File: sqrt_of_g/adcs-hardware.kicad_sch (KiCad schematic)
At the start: 29 parts, among them J10 35362-0650, J11 Conn_01x10, J12 353620850, J13 35362-0650, J14 353621050, J15 Conn_01x10, J16 35362-0650, J17 Conn_01x10, J18 35362-0650, J19 353621050, J20 353621050, J21 Conn_01x06, J22 Conn_01x06, J23 Conn_01x06, J24 Conn_01x06, J25 Conn_01x06, J26 Conn_01x06, J27 Conn_01x10, J28 35362-0650, J6 Conn_01x06, J7 Conn_01x08, J8 Conn_01x10, J9 35362-0650

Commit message: update board
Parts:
- J11, J15, J17, J27, J8: footprint (none) -> Connector_PinHeader_1.27mm:PinHeader_1x10_P1.27mm_Vertical
- J14: value 353621050 -> Thruster
- J21, J22, J23, J24, J25, J26: footprint (none) -> mainboard:MOLEX_35362-0650
- J7: footprint (none) -> Connector_PinHeader_2.54mm:PinHeader_1x08_P2.54mm_Vertical
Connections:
- net RX_ADCS renamed RX_FROM_PYCUBED
- net TX_ADCS renamed TX_TO_PYCUBED
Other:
- sheet GPS ports: added RX_FROM_MICRO, TX_TO_MICRO; removed RX_GPS, TX_GPS
- note added: "2-3. Add jumpers to allow USB battery power to Teensy (for programming). DO NOT USE TO POWER THRUSTER, COILS, or WHEELS."
- note added: "@GRANT this uses a sheet field to pass in 100k for the source resistor"
- note added: "Connector allows the RBFs placement on a side panel"
- note added: "LDO for analog 3V3 supply? add inductor, caps to filter things out? Should I make an analog GND plane? I feel like I am fine."
- note added: "LPUART4"
- note added: "Power Harness and Power Enable"
- note added: "RBF Jumpers / Harness"
- note added: "This power enable can hard reset the whole board."
- note removed: "2-3. Add jumper to allow USB battery power to wheels, coils. DO NOT USE TO POWER THRUSTER"
- note removed: "@GRANT this uses a sheet field to pass in 100k for the source resistor Somewhat related: should we power this from VBATT_IN (to avoid having two enables in series )? This is already after the foot switches"
- note removed: "ADCS Enable"
- note removed: "Connector allows the RBFs to be placed on a side panel"
- note removed: "From the board's POV, this is where it recieves and transmits. These must be flipped on the PyCubed side"
- note removed: "LDO for analog 3V3 supply? add inductor, caps to filter things out? Should I make an analog GND? I feel like I am fine."
- note removed: "RBF Jumpers"

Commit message: update main board
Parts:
- removed J10, J13, J16, J18: 35362-0650, mainboard:MOLEX_35362-0650, symbol mainboard:35362-0650
- removed J15, J17, J8: Conn_01x10, Connector_PinHeader_1.27mm:PinHeader_1x10_P1.27mm_Vertical, symbol Connector_Generic:Conn_01x10
- removed J19, J20: 353621050, CON_353621050, symbol adcs:353621050
- added H1, H2, H3, H4: MountingHole_Pad, MountingHole:MountingHole_3.2mm_M3_DIN965_Pad, symbol Mechanical:MountingHole_Pad
- added J1, J2: 353620650, mainboard:MOLEX_35362-0650, symbol mainboard:35362-0650
- added J12, J13, J14: Conn_01x10, Connector_PinHeader_2.54mm:PinHeader_1x10_P2.54mm_Vertical, symbol Connector_Generic:Conn_01x10
- added J3, J4: 353620850, adcs:SHDR8W50P0X200_1X8_1830X550X850P, symbol Connector_Generic:Conn_01x08
- added L1: 330uH, adcs:IND_SRN6045TA-331K, symbol Device:L
- J10: renamed from J14; value Thruster -> Thruster Connector; Flight (none) -> 353621050; Manufacturer_Name (none) -> Molex
- J11: footprint Connector_PinHeader_1.27mm:PinHeader_1x10_P1.27mm_Vertical -> Connector_PinHeader_2.54mm:PinHeader_1x10_P2.54mm_Vertical
- J15: renamed from J23; value Conn_01x06 -> 353620650; Flight (none) -> 353620650; Manufacturer_Name (none) -> Molex
- J16: renamed from J24; value Conn_01x06 -> 353620650; Flight (none) -> 353620650; Manufacturer_Name (none) -> Molex
- J17: renamed from J21; value Conn_01x06 -> 353620650; Flight (none) -> 353620650; Manufacturer_Name (none) -> Molex
- J18: renamed from J22; value Conn_01x06 -> 353620650; Flight (none) -> 353620650; Manufacturer_Name (none) -> Molex
- J19: renamed from J25; value Conn_01x06 -> 353620650; Flight (none) -> 353620650; Manufacturer_Name (none) -> Molex
- J20: renamed from J26; value Conn_01x06 -> 353620650; Flight (none) -> 353620650; Manufacturer_Name (none) -> Molex
- J21: renamed from J27; footprint Connector_PinHeader_1.27mm:PinHeader_1x10_P1.27mm_Vertical -> Connector_PinHeader_2.54mm:PinHeader_1x10_P2.54mm_Vertical
- J5: renamed from J28; value 35362-0650 -> 353620650; Flight (none) -> 353620650; Manufacturer_Name (none) -> Molex
- J6: renamed from J9; value 35362-0650 -> 353620650; Flight (none) -> 353620650; Manufacturer_Name (none) -> Molex
- J8: renamed from J7; value Conn_01x08 -> Control Debug Header; DNI (none) -> DNI
- J9: renamed from J12; footprint mainboard:353620850 -> adcs:SHDR8W50P0X200_1X8_1830X550X850P; Flight (none) -> 353620850; Manufacturer_Name (none) -> Molex
- J?: renamed from J6; Flight (none) -> PH1RB-06-UA; Manufacturer_Name (none) -> Adam-Tech
- renumbered R27 to R?
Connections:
- net 3V3_PD1: now also J2.1, J3.1 (Pin_1), J3.5 (Pin_5)
- net 3V3_PD2: now also J1.1, J4.1 (Pin_1), J4.5 (Pin_5)
- net GND: now also H1.1, H2.1, H3.1, H4.1, J1.2, J12.10 (Pin_10), J13.10 (Pin_10), J14.10 (Pin_10), J2.2, J3.2 (Pin_2), J3.6 (Pin_6), J4.2 (Pin_2), J4.6 (Pin_6); no longer J6.1, J6.3, J6.5
- net MCU/GPIO_AD_B0_12: now also J3.3 (Pin_3)
- net MCU/GPIO_AD_B0_13: now also J3.4 (Pin_4)
- net MCU/GPIO_AD_B0_14: now also J3.7 (Pin_7)
- net MCU/GPIO_AD_B0_15: now also J3.8 (Pin_8)
- net MCU/GPIO_AD_B1_00: now also J2.3
- net MCU/GPIO_AD_B1_01: now also J2.4
- net MCU/GPIO_AD_B1_04: now also J2.5
- net MCU/GPIO_AD_B1_05: now also J2.6
- net MCU/GPIO_AD_B1_06: now also J4.3 (Pin_3)
- net MCU/GPIO_AD_B1_07: now also J4.4 (Pin_4)
- net MCU/GPIO_AD_B1_08: now also J4.7 (Pin_7)
- net MCU/GPIO_AD_B1_09: now also J4.8 (Pin_8)
- net MCU/GPIO_AD_B1_10: now also J1.3
- net MCU/GPIO_AD_B1_11: now also J1.4
- net MCU/GPIO_AD_B1_12: now also J1.5
- net MCU/GPIO_AD_B1_13: now also J1.6
- net MCU/GPIO_AD_B1_14: now also J14.5 (Pin_5)
- net MCU/GPIO_AD_B1_15: now also J14.6 (Pin_6)
- net MCU/GPIO_B0_08: now also J13.1 (Pin_1)
- net MCU/GPIO_B0_09: now also J13.2 (Pin_2)
- net MCU/GPIO_B0_10: now also J13.3 (Pin_3)
- net MCU/GPIO_B0_11: now also J13.4 (Pin_4)
- net MCU/GPIO_B0_12: now also J13.5 (Pin_5)
- net MCU/GPIO_B0_14: now also J13.6 (Pin_6)
- net MCU/GPIO_B1_02: now also J12.1 (Pin_1); no longer J11.1 (Pin_1)
- net MCU/GPIO_B1_03: now also J12.2 (Pin_2); no longer J11.2 (Pin_2)
- net MCU/GPIO_B1_04: now also J12.3 (Pin_3); no longer J11.3 (Pin_3)
- net MCU/GPIO_B1_05: now also J12.4 (Pin_4); no longer J11.4 (Pin_4)
- net MCU/GPIO_B1_07: now also J12.5 (Pin_5); no longer J11.5 (Pin_5)
- net MCU/GPIO_B1_09: now also J12.6 (Pin_6); no longer J11.6 (Pin_6)
- net MCU/GPIO_B1_10: now also J11.1 (Pin_1)
- net MCU/GPIO_B1_11: now also J11.2 (Pin_2)
- net MCU/GPIO_B1_12: now also J11.3 (Pin_3)
- net MCU/GPIO_B1_13: now also J11.4 (Pin_4)
- net MCU/GPIO_B1_14: now also J11.5 (Pin_5)
- net MCU/GPIO_B1_15: now also J11.6 (Pin_6)
- net MCU/GPIO_EMC_00: now also J11.7 (Pin_7)
- net MCU/GPIO_EMC_03: now also J11.8 (Pin_8)
- net MCU/GPIO_EMC_04: now also J11.9 (Pin_9)
- net MCU/GPIO_EMC_18: now also J12.7 (Pin_7); no longer J11.7 (Pin_7)
- net MCU/GPIO_EMC_19: now also J12.8 (Pin_8); no longer J11.8 (Pin_8)
- net MCU/GPIO_EMC_20: now also J12.9 (Pin_9); no longer J11.9 (Pin_9)
- net MCU/GPIO_EMC_21: now also J13.7 (Pin_7)
- net MCU/GPIO_EMC_30: now also J13.9 (Pin_9)
- net MCU/GPIO_EMC_31: now also J14.7 (Pin_7)
- net MCU/GPIO_EMC_32: now also J14.8 (Pin_8)
- net MCU/GPIO_EMC_33: now also J14.9 (Pin_9)
- net MCU/GPIO_SD_B1_00: now also J14.1 (Pin_1)
- net MCU/GPIO_SD_B1_01: now also J14.2 (Pin_2)
- net MCU/GPIO_SD_B1_02: now also J14.3 (Pin_3)
- net MCU/GPIO_SD_B1_03: now also J14.4 (Pin_4)
- new net ADCS Power Enable/VBUS_IN: L1.2
- new net VBATT_IN: J6.1, J6.3, J6.5, L1.1
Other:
- note added: "1"
- note added: "2"
- note added: "3"
- note added: "4"
- note added: "Mounting Holes"
- note removed: "A"
- note removed: "B"
- note removed: "C"
- note removed: "D"
- note removed: "See motors.kicad_sch for work-in-progress motor controller schematic. In the end, we likely do not need all this GPIO per motor."

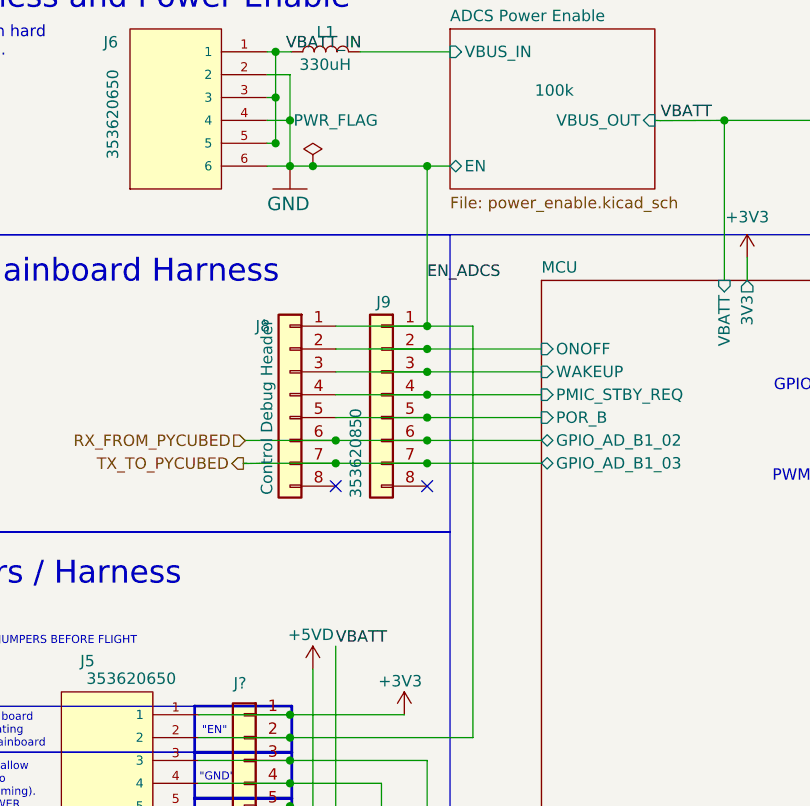
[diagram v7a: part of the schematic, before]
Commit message: don't ground enable pin
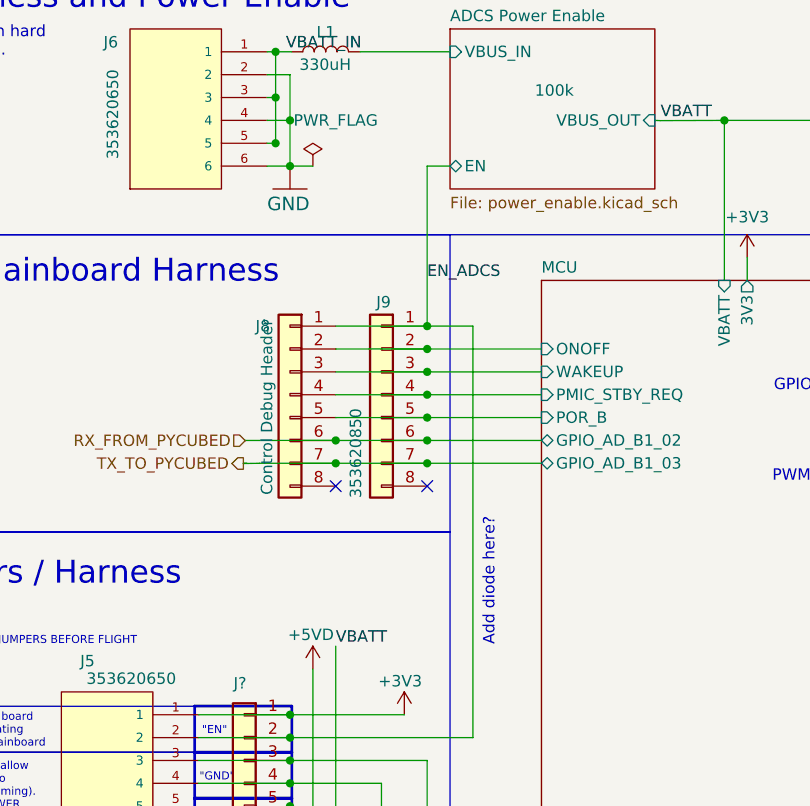
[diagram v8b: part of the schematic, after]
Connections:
- net GND: no longer J5.2, J8.1 (Pin_1), J9.1 (Pin_1), J?.2 (Pin_2)
- new net EN_ADCS: J5.2, J8.1 (Pin_1), J9.1 (Pin_1), J?.2 (Pin_2)
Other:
- note added: "Add diode here?"
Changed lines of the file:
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@@
   (junction (at 175.26 157.48) (diameter 0) (color 0 0 0 0)
   )
-  (junction (at 91.44 48.26) (diameter 0) (color 0 0 0 0)
-  )
   (junction (at 60.96 243.84) (diameter 0) (color 0 0 0 0)
   )
@@
   )
   (junction (at 91.44 68.58) (diameter 0) (color 0 0 0 0)
-  )
-  (junction (at 78.74 48.26) (diameter 0) (color 0 0 0 0)
   )
   (junction (at 172.72 137.16) (diameter 0) (color 0 0 0 0)
@@
     (stroke (width 0) (type default))
   )
-  (wire (pts (xy 78.74 48.26) (xy 91.44 48.26))
-    (stroke (width 0) (type default))
-  )
   (wire (pts (xy 74.5998 45.72) (xy 73.66 45.72))
     (stroke (width 0) (type default))
@@
     (effects (font (size 2.54 2.54)) (justify right bottom))
   )
+  (text "Add diode here?" (at 99.06 101.6 90)
+    (effects (font (size 1.27 1.27)) (justify left bottom))
+  )
   (text "PyCubed Mainboard Harness" (at 24.8158 61.5442 0)
